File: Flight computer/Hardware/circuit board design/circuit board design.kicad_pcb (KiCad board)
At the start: 4 copper layers, 30.5 x 82.6 mm, 89 parts, among them J1 Conn_01x05, J2 USB_B_Micro, J3 Screw_Terminal_01x04, J4 Conn_01x02, J5 Screw_Terminal_01x04, J6 Conn_Coaxial, J7 Conn_Coaxial, U1 IIS2MDC, U10 BMI088, U11 ATSAML21J18B-AUT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

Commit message: moved the caps out of the courtyard of the accl/gyro sensor
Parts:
- added G***: LOGO, flight-computer:ICSS_Logo, B.Cu at (108.1, 125.6)
- moved C28 0.25 mm to (95.1, 129.3)
- moved C29 0.25 mm to (93.6, 129.3)
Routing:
- net +3V3: track 306.9 -> 307.6 mm
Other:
- board text added: "Rocket Flight Computer v1.0 Medad Newman, Richard Ibbotson 2019"

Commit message: Precisely aligned the mounting holes
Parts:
- moved G*** 53.7 mm to (107.2, 71.9)
- moved H2 0.18 mm to (119.0, 61.6)
- moved H1 0.13 mm to (96.1, 61.6)
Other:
- board text added: "Rocket Flight Computer v1.0 Imperial College Space Society Medad Newman, Richard Ibbotson Sept 2019"
- board text removed: "Rocket Flight Computer v1.0 Medad Newman, Richard Ibbotson 2019"
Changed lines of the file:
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@@
   )
   (layers
-    (0 F.Cu signal)
+    (0 F.Cu signal hide)
     (1 GND.Cu power hide)
     (2 VCC.Cu power hide)
-    (31 B.Cu signal hide)
+    (31 B.Cu signal)
     (32 B.Adhes user hide)
     (33 F.Adhes user hide)
@@
     (35 F.Paste user hide)
     (36 B.SilkS user)
-    (37 F.SilkS user)
+    (37 F.SilkS user hide)
     (38 B.Mask user)
     (39 F.Mask user hide)
@@
       (padsonsilk false)
       (subtractmaskfromsilk false)
-      (outputformat 1)
+      (outputformat 4)
       (mirror false)
-      (drillshape 1)
+      (drillshape 0)
       (scaleselection 1)
-      (outputdirectory ""))
+      (outputdirectory "D:/Long term storage and temp/dead weight program downloads/gerber test/"))
   )
   (net 0 "")
@@
   )
   (module flight-computer:ICSS_Logo (layer B.Cu)
-    (at 108.077 125.603 180)
-    (fp_text reference G*** (at 0 0) (layer B.SilkS) hide
+    (at 107.188 71.882 180)
+    (fp_text reference G*** (at -0.127 5.08) (layer B.SilkS) hide
       (effects (font (size 1.524 1.524) (thickness 0.3)) (justify mirror))
     )
@@
   )
   (module MountingHole:MountingHole_3.2mm_M3_Pad (layer F.Cu)
-    (at 119.126 61.468 270)
+    (at 118.999 61.595 270)
     (descr "Mounting Hole 3.2mm, M3")
     (tags "mounting hole 3.2mm m3")
@@
   )
   (module MountingHole:MountingHole_3.2mm_M3_Pad (layer F.Cu)
-    (at 96.012 61.595 270)
+    (at 96.139 61.595 270)
     (descr "Mounting Hole 3.2mm, M3")
     (tags "mounting hole 3.2mm m3")
@@
     )
   )
-  (gr_text "Rocket Flight Computer v1.0\nMedad Newman, Richard Ibbotson 2019" (at 107.569 131.318) (layer B.SilkS)
+  (gr_text "Rocket Flight Computer v1.0\nImperial College Space Society\nMedad Newman, Richard Ibbotson\nSept 2019" (at 107.569 127.635) (layer B.SilkS)
     (effects (font (size 1 1) (thickness 0.15)) (justify mirror))
   )

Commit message: done for today
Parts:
- removed G***: LOGO, flight-computer:ICSS_Logo
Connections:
- U11 pad 10: Net-(J8-Pad2) -> (no net)
- U11 pad 9: Net-(J8-Pad1) -> (no net)

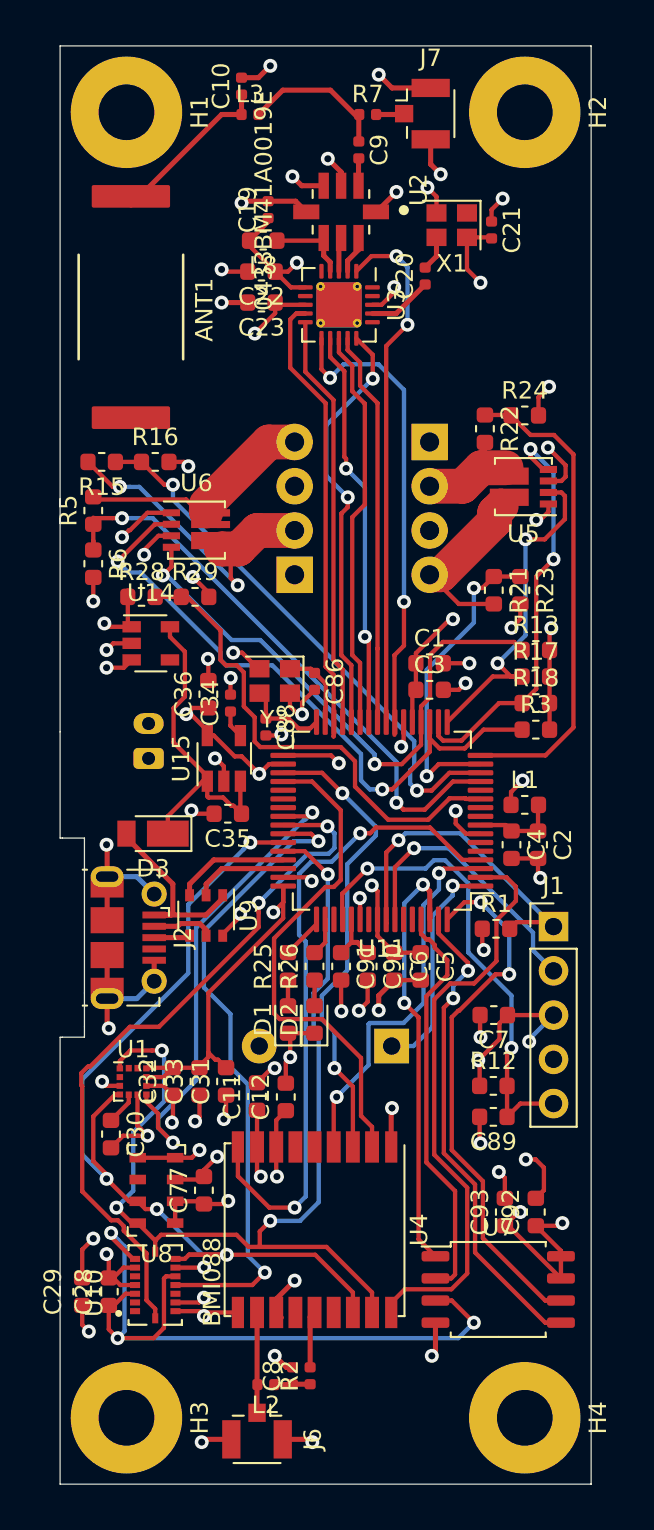
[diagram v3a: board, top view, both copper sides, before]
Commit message: added in crystal footprint
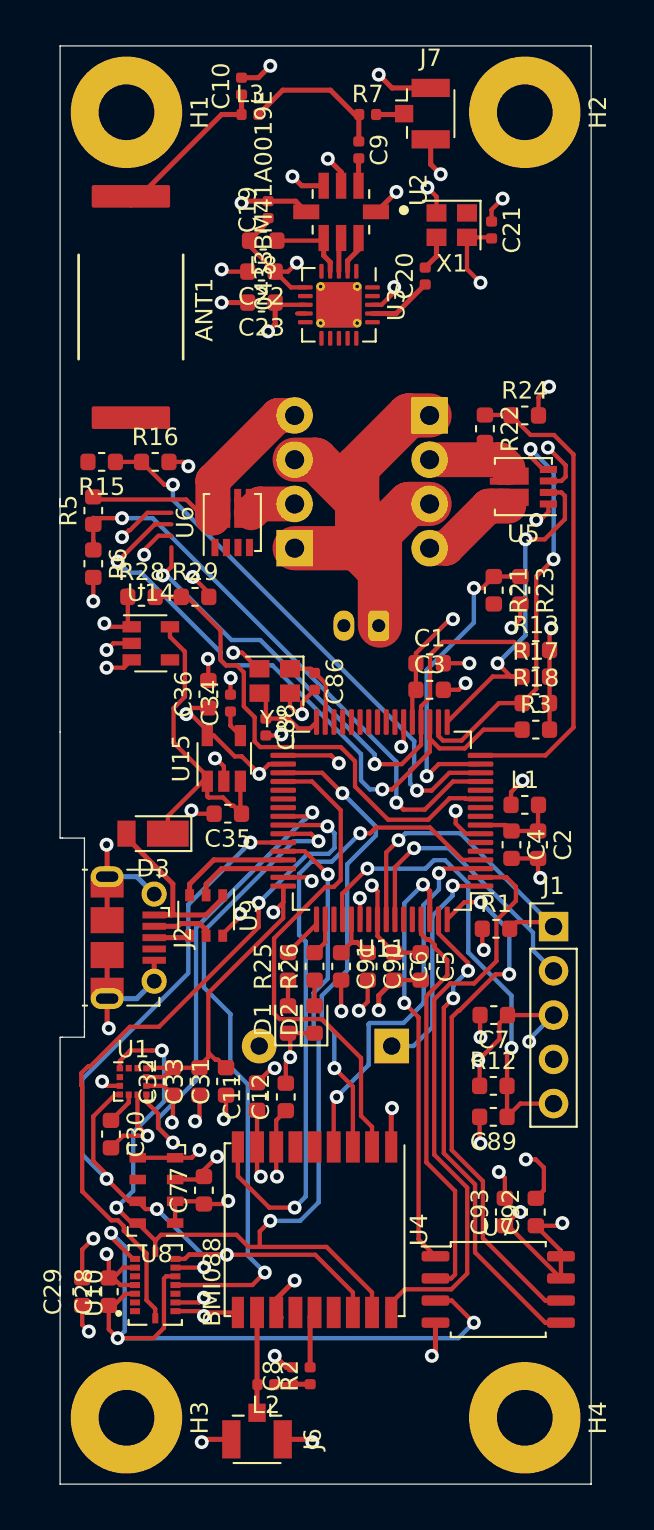
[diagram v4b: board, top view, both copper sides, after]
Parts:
- moved J4 15.2 mm to (110.6, 91.1), turned to 180 degrees
- moved U6 2.10 mm to (102.2, 85.1), turned to 90 degrees
- moved J3 1.52 mm to (105.8, 86.6)
- moved J5 1.52 mm to (113.5, 79.0)
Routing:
- net Vdrive: track 5.46 -> 74.8 mm
- net /MCU/MCU_PB11: track 30.2 -> 0.00 mm, vias 2 -> 0
- net /MCU/MCU_PB10: track 27.7 -> 0.00 mm, vias 2 -> 0
- net /MCU/MCU_PA13: track 26.5 -> 0.47 mm
- net /MCU/MCU_NSEL1: track 24.4 -> 0.00 mm, vias 2 -> 0
- net /MCU/MCU_PA12: track 23.8 -> 0.00 mm
- net /MCU/MCU_MISO1: track 23.1 -> 0.00 mm
- net /MCU/MCU_SCLK1: track 22.9 -> 0.00 mm, vias 2 -> 0
- net /MCU/MCU_MOSI1: track 22.7 -> 0.00 mm
- net +3V3: track 307.6 -> 285.9 mm
- net /pyro_driver/FET_B: track 18.7 -> 2.71 mm, vias 2 -> 0
- net /pyro_driver/FET_C: track 10.4 -> 5.55 mm
- net /pyro_driver/FET_A: track 13.6 -> 15.7 mm
- net /pyro_driver/FET_D: track 6.37 -> 4.69 mm
- added copper zone on VCC.Cu, net +3V3
- removed copper zone on VCC.Cu, net Vdrive
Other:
- net class FETs added: clearance 0.2, trace_width 2, via_dia 0.8, via_drill 0.4
- net class Power added: clearance 0.2, trace_width 2.54, via_dia 0.8, via_drill 0.4

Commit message: routed most of the board
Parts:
- Y3: footprint Crystal:Crystal_SMD_2520-4Pin_2.5x2.0mm -> flight-computer:Crystal_SMD_2520-4Pin_2.5x2.0mm
- moved R15 9.97 mm to (100.5, 89.8), turned to 0 degrees
- moved R16 8.14 mm to (97.4, 89.8), turned to 180 degrees
- moved U14 6.93 mm to (104.3, 90.4), turned to 270 degrees
- moved R28 4.01 mm to (100.5, 91.4), turned to 180 degrees
- moved R29 3.37 mm to (97.4, 91.4), turned to 180 degrees
- moved U6 1.89 mm to (100.3, 85.3)
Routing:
- net /MCU/MCU_NSEL1: track 0.00 -> 38.2 mm, vias 0 -> 2
- net /MCU/MCU_PB10: track 0.00 -> 32.0 mm, vias 0 -> 2
- net /MCU/MCU_PB11: track 0.00 -> 30.4 mm, vias 0 -> 2
- net /MCU/MCU_PA13: track 0.47 -> 27.3 mm, vias 0 -> 2
- net /MCU/MCU_SCLK1: track 0.00 -> 26.6 mm, vias 0 -> 2
- net /MCU/MCU_PA12: track 0.00 -> 25.6 mm, vias 0 -> 2
- net /MCU/MCU_MOSI1: track 0.00 -> 24.5 mm, vias 0 -> 2
- net /MCU/MCU_MISO1: track 0.00 -> 24.0 mm, vias 0 -> 2
- net Vdrive: track 74.8 -> 53.2 mm, vias 2 -> 0
- net /pyro_driver/FET_C: track 5.55 -> 11.4 mm
- net /MCU/MCU_PA06: track 18.2 -> 23.1 mm
- net /pyro_driver/FIRE_A: track 38.4 -> 34.1 mm
- net /pyro_driver/FET_A: track 15.7 -> 18.5 mm
- net /pyro_driver/FET_B: track 2.71 -> 0.00 mm
- net /MCU/MCU_PA04: track 33.2 -> 35.3 mm
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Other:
- net class Power: trace_width 2.54 -> 2

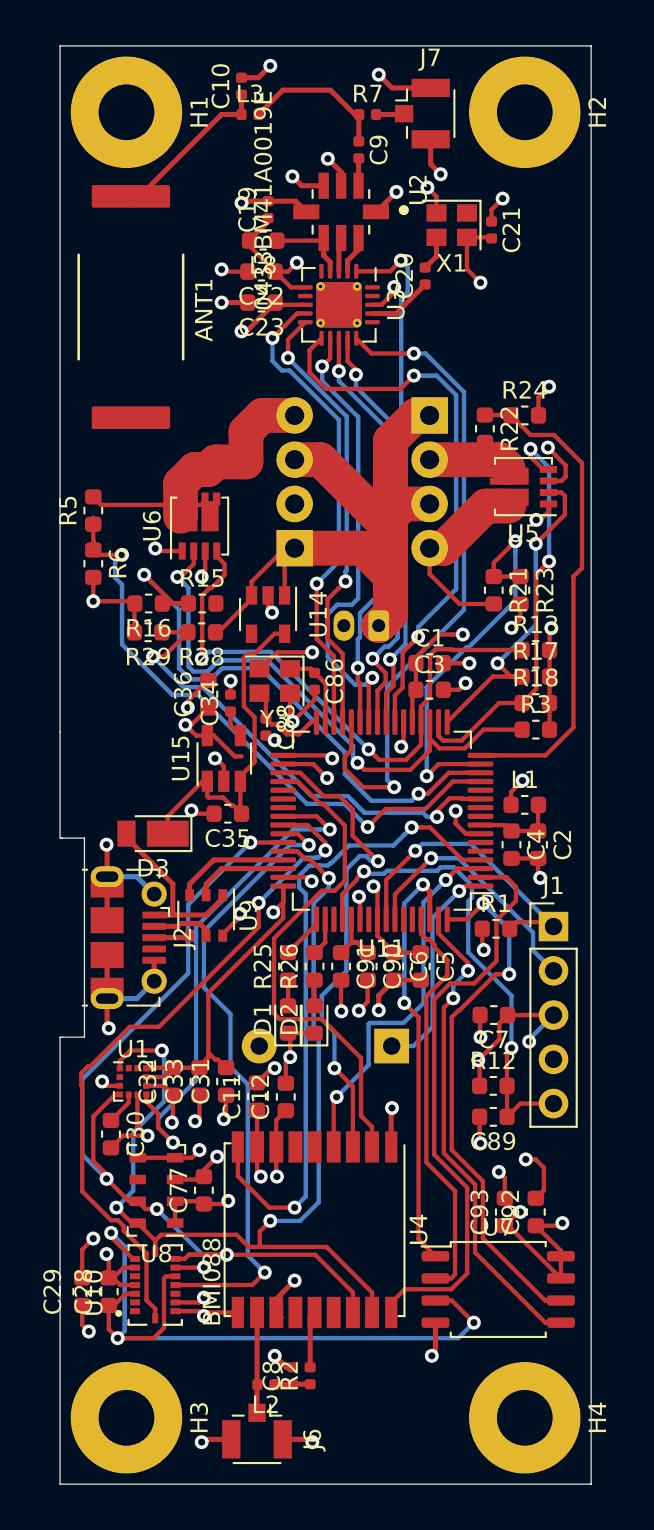
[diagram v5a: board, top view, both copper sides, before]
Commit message: Finished routing the board with 3.3V power plane
Power for mosfets comes from 2mm tracks on top layer. Todo: make their connection to ground more robust
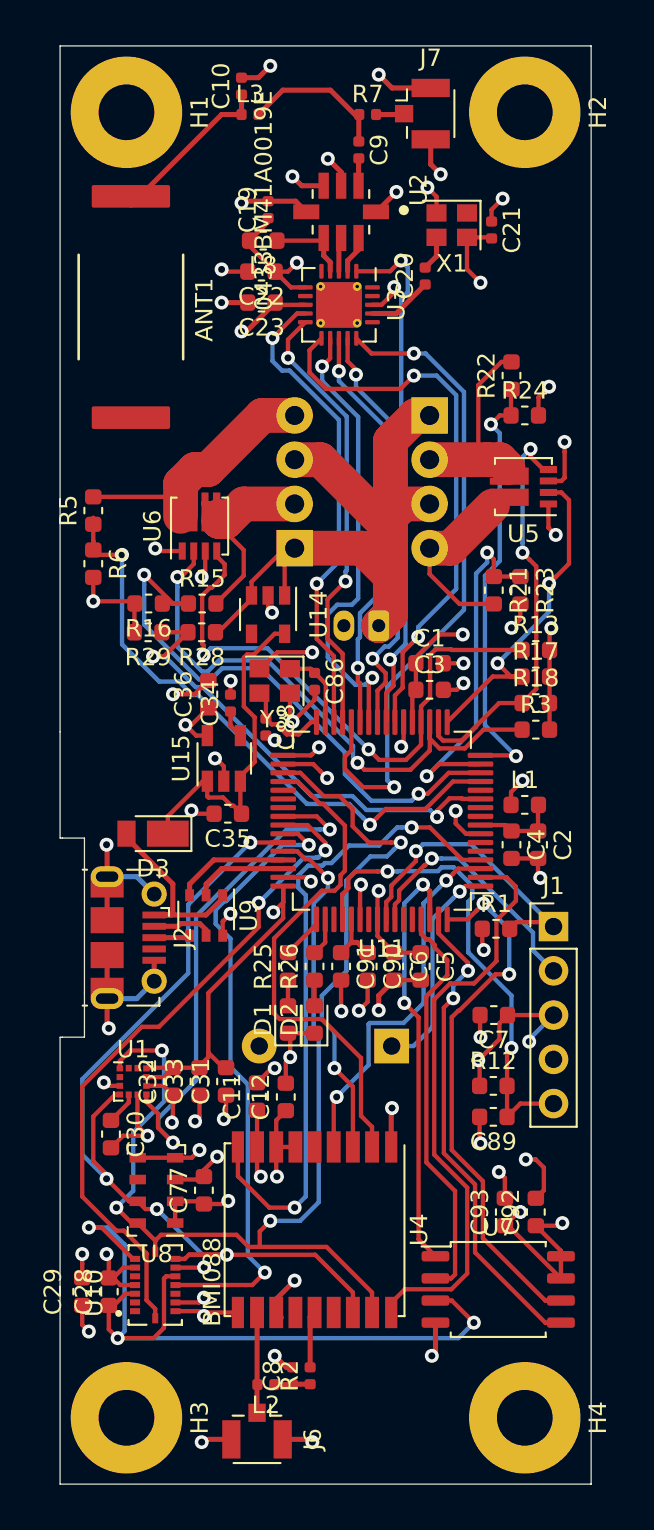
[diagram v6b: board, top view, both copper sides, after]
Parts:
- moved R22 3.41 mm to (118.2, 76.7), turned to 90 degrees
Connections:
- U4 pad 6: (no net) -> +3V3
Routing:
- net /pyro_driver/FET_B: track 0.00 -> 11.5 mm
- net +3V3: track 286.3 -> 278.7 mm
- net /pyro_driver/FET_D: track 4.69 -> 11.6 mm
- net /pyro_driver/FET_A: track 18.5 -> 15.6 mm
- net /MCU/MCU_PA07: track 28.1 -> 25.3 mm, vias 0 -> 2
- net /MCU/MCU_PA06: track 23.1 -> 20.7 mm
- net /gps/GPS_RXD: track 27.9 -> 29.6 mm
- net GND: track 159.7 -> 158.6 mm
- net /pyro_driver/FET_C: track 11.4 -> 10.5 mm

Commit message: Flood fill top and bottom layer
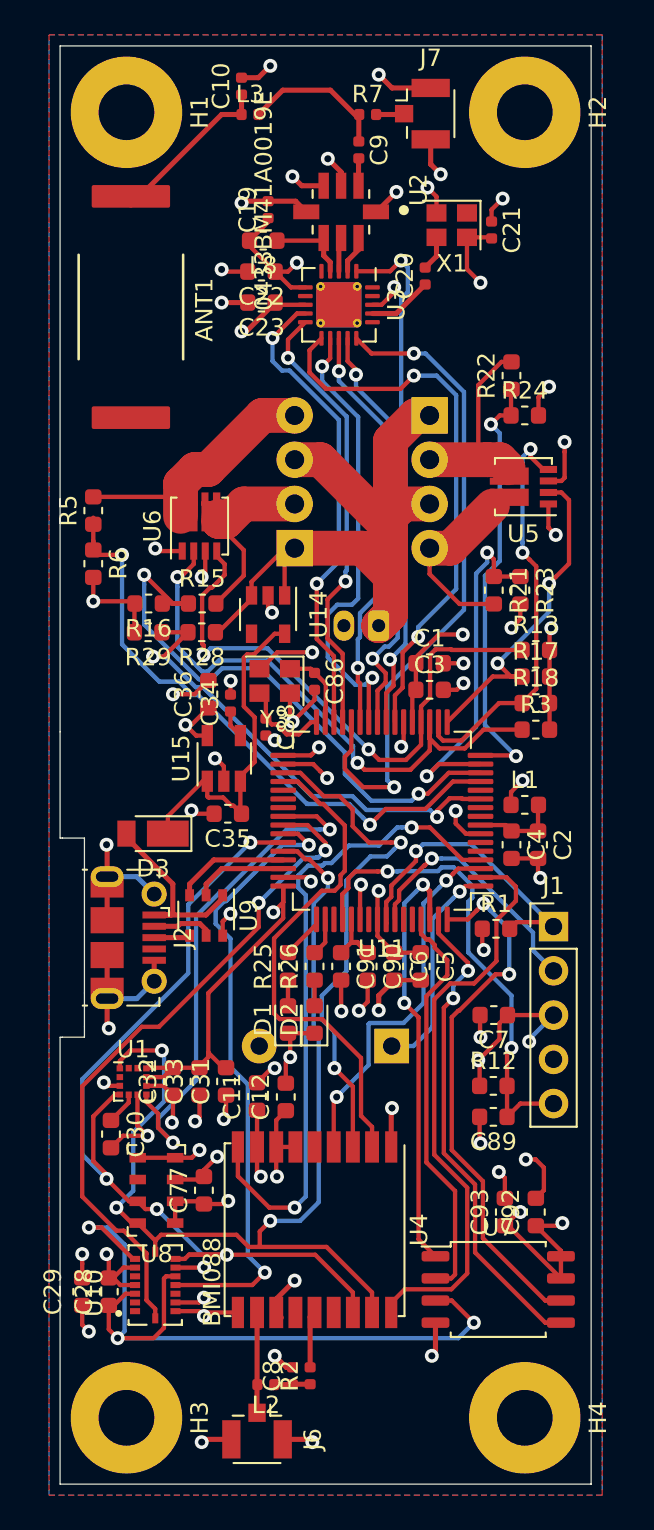
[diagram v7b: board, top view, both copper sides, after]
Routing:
- added copper zone on B.Cu, net GND
- added copper zone on F.Cu, net GND
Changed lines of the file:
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@@
   (layers
     (0 F.Cu signal)
-    (1 GND.Cu power hide)
-    (2 VCC.Cu power hide)
+    (1 GND.Cu power)
+    (2 VCC.Cu power)
     (31 B.Cu signal)
     (32 B.Adhes user hide)
@@
       )
     )
+  )
+  (zone (net 1) (net_name GND) (layer F.Cu) (hatch edge 0.508)
+    (connect_pads (clearance 0.508))
+    (min_thickness 0.254)
+    (fill yes (arc_segments 32) (thermal_gap 0.508) (thermal_bridge_width 0.508))
+    (polygon
+      (pts
+        (xy 91.694 57.15) (xy 91.694 140.97) (xy 123.444 140.97) (xy 123.444 57.15)
+      )
+    )
+  )
+  (zone (net 1) (net_name GND) (layer B.Cu) (hatch edge 0.508)
+    (connect_pads (clearance 0.508))
+    (min_thickness 0.254)
+    (fill yes (arc_segments 32) (thermal_gap 0.508) (thermal_bridge_width 0.508))
+    (polygon
+      (pts
+        (xy 91.694 57.15) (xy 123.444 57.15) (xy 123.444 140.97) (xy 91.694 140.97)
+      )
+    )
